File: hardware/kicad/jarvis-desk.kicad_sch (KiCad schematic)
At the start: 4 parts, among them J1 RJ12_6P6C, U1 Beetle_ESP32-C6

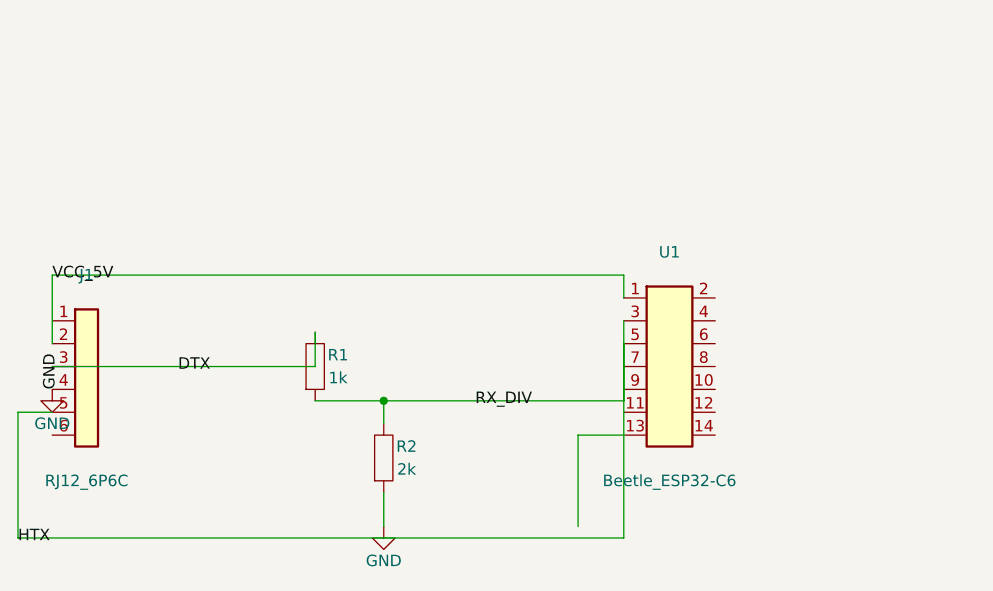
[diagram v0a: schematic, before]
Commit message: Rebuild PCB with official DFRobot Beetle ESP32-C6 footprint
- Copy official kicad_mod and kicad_sym from DFRobot to hardware/kicad/libs/
- Rewrite PCB (38x30mm board) using official 16-pin Beetle footprint
  with correct pad positions (2x8, 2.54mm pitch, 17.78mm row spacing)
- Update schematic to use official Beetle_ESP32-C6 symbol
- Route all nets: GND, VCC_5V, DTX→R1→R2 voltage divider→GPIO17,
  HTX→GPIO16, with back copper GND pour
- Change DESK_TX_PIN from 18 to 16 in config.h and config.example.h
  (GPIO18 not on Beetle headers; GPIO16 is pin 12, adjacent to GPIO17)
- Pin assignments: GPIO17 (pin 13) = RX, GPIO16 (pin 12) = TX

Co-authored-by: Copilot <223556219+Copilot@users.noreply.github.com>
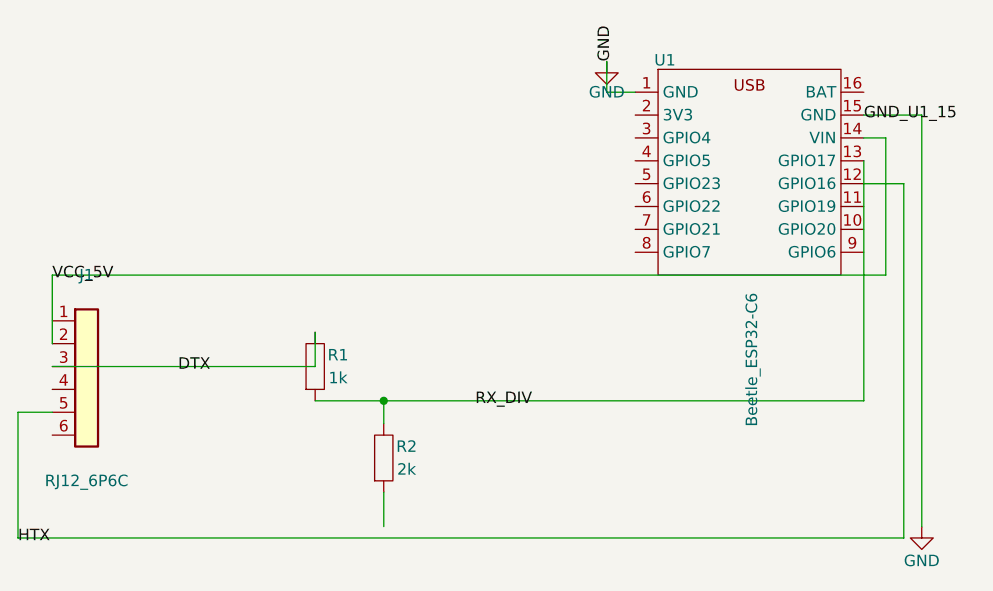
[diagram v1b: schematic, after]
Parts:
- U1: footprint Connector_PinHeader_2.54mm:PinHeader_2x07_P2.54mm_Vertical -> libs:Beetle_ESP32-C6; symbol Connector_Generic:Conn_02x07_Odd_Even -> beetle_esp32_c6:Beetle_ESP32-C6
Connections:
- net GND: now also U1.1 (GND), U1.15 (GND); no longer J1.4 (Pin_4), R2.2
- net HTX: now also U1.12 (GPIO16); no longer R1.2, R2.1, U1.3 (Pin_3), U1.5 (Pin_5)
- net VCC_5V: now also U1.14 (VIN); no longer U1.1 (Pin_1)
- net RX_DIV: now reaches U1.13 (GPIO17)
- net RX_DIV: now also R1.2, R2.1
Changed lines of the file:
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@@
   )
   (symbol
-    (lib_id "Connector_Generic:Conn_02x07_Odd_Even")
-    (at 139.7 88.9 0)
+    (lib_id "beetle_esp32_c6:Beetle_ESP32-C6")
+    (at 139.7 78.74 0)
     (unit 1)
     (exclude_from_sim no)
@@
     (on_board yes)
     (dnp no)
-    (property "Reference" "U1" (at 140.97 76.2 0) (effects (font (size 1.27 1.27))))
-    (property "Value" "Beetle_ESP32-C6" (at 140.97 101.6 0) (effects (font (size 1.27 1.27))))
-    (property "Footprint" "Connector_PinHeader_2.54mm:PinHeader_2x07_P2.54mm_Vertical" (at 139.7 88.9 0) (effects (font (size 1.27 1.27)) hide))
-    (property "Datasheet" "~" (at 139.7 88.9 0) (effects (font (size 1.27 1.27)) hide))
+    (property "Reference" "U1" (at 140.462 54.864 0) (effects (font (size 1.27 1.27))))
+    (property "Value" "Beetle_ESP32-C6" (at 150.114 88.138 90) (effects (font (size 1.27 1.27))))
+    (property "Footprint" "libs:Beetle_ESP32-C6" (at 139.7 72.39 0) (effects (font (size 1.27 1.27)) hide))
+    (property "Datasheet" "" (at 139.7 72.39 0) (effects (font (size 1.27 1.27)) hide))
     (pin "1")
     (pin "2")
@@
     (pin "13")
     (pin "14")
+    (pin "15")
+    (pin "16")
     (instances
       (project "jarvis-desk"
@@
   (symbol
     (lib_id "power:GND")
-    (at 72.39 91.44 0)
+    (at 134 55 0)
     (unit 1)
     (exclude_from_sim no)
@@
     (on_board yes)
     (dnp no)
-    (property "Reference" "#PWR01" (at 72.39 97.79 0) (effects (font (size 1.27 1.27)) hide))
-    (property "Value" "GND" (at 72.39 95.25 0) (effects (font (size 1.27 1.27))))
-    (property "Footprint" "" (at 72.39 91.44 0) (effects (font (size 1.27 1.27)) hide))
-    (property "Datasheet" "" (at 72.39 91.44 0) (effects (font (size 1.27 1.27)) hide))
+    (property "Reference" "#PWR01" (at 134 61.34 0) (effects (font (size 1.27 1.27)) hide))
+    (property "Value" "GND" (at 134 58.42 0) (effects (font (size 1.27 1.27))))
+    (property "Footprint" "" (at 134 55 0) (effects (font (size 1.27 1.27)) hide))
+    (property "Datasheet" "" (at 134 55 0) (effects (font (size 1.27 1.27)) hide))
     (pin "1")
     (instances
@@
   (symbol
     (lib_id "power:GND")
-    (at 109.22 106.68 0)
+    (at 169 106.68 0)
     (unit 1)
     (exclude_from_sim no)
@@
     (on_board yes)
     (dnp no)
-    (property "Reference" "#PWR02" (at 109.22 113.03 0) (effects (font (size 1.27 1.27)) hide))
-    (property "Value" "GND" (at 109.22 110.49 0) (effects (font (size 1.27 1.27))))
-    (property "Footprint" "" (at 109.22 106.68 0) (effects (font (size 1.27 1.27)) hide))
-    (property "Datasheet" "" (at 109.22 106.68 0) (effects (font (size 1.27 1.27)) hide))
+    (property "Reference" "#PWR02" (at 169 113.03 0) (effects (font (size 1.27 1.27)) hide))
+    (property "Value" "GND" (at 169 110.49 0) (effects (font (size 1.27 1.27))))
+    (property "Footprint" "" (at 169 106.68 0) (effects (font (size 1.27 1.27)) hide))
+    (property "Datasheet" "" (at 169 106.68 0) (effects (font (size 1.27 1.27)) hide))
     (pin "1")
     (instances
@@
     (stroke (width 0) (type default))
   )
-  (wire (pts (xy 109.22 92.71) (xy 135.89 92.71))
+  (wire (pts (xy 109.22 92.71) (xy 162.56 92.71))
     (stroke (width 0) (type default))
   )
-  (wire (pts (xy 135.89 92.71) (xy 135.89 86.36))
+  (wire (pts (xy 162.56 92.71) (xy 162.56 66.04))
     (stroke (width 0) (type default))
   )
@@
     (stroke (width 0) (type default))
   )
-  (wire (pts (xy 72.39 78.74) (xy 135.89 78.74))
+  (wire (pts (xy 72.39 78.74) (xy 165 78.74))
     (stroke (width 0) (type default))
   )
-  (wire (pts (xy 135.89 78.74) (xy 135.89 81.28))
+  (wire (pts (xy 165 78.74) (xy 165 63.5))
+    (stroke (width 0) (type default))
+  )
+  (wire (pts (xy 165 63.5) (xy 162.56 63.5))
     (stroke (width 0) (type default))
   )
@@
     (stroke (width 0) (type default))
   )
-  (wire (pts (xy 68.58 107.95) (xy 135.89 107.95))
+  (wire (pts (xy 68.58 107.95) (xy 167 107.95))
     (stroke (width 0) (type default))
   )
-  (wire (pts (xy 135.89 107.95) (xy 135.89 83.82))
+  (wire (pts (xy 167 107.95) (xy 167 68.58))
     (stroke (width 0) (type default))
   )
-  (wire (pts (xy 135.89 96.52) (xy 130.81 96.52))
+  (wire (pts (xy 167 68.58) (xy 162.56 68.58))
     (stroke (width 0) (type default))
   )
-  (wire (pts (xy 130.81 96.52) (xy 130.81 106.68))
+  (wire (pts (xy 162.56 60.96) (xy 169 60.96))
+    (stroke (width 0) (type default))
+  )
+  (wire (pts (xy 169 60.96) (xy 169 106.68))
+    (stroke (width 0) (type default))
+  )
+  (wire (pts (xy 137.16 58.42) (xy 134 58.42))
+    (stroke (width 0) (type default))
+  )
+  (wire (pts (xy 134 58.42) (xy 134 55))
     (stroke (width 0) (type default))
   )
@@
   )
   (label "GND"
-    (at 72.39 91.44 270)
+    (at 134 55 270)
     (effects (font (size 1.27 1.27)) (justify left))
   )
@@
     (effects (font (size 1.27 1.27)) (justify left))
   )
+  (label "GND_U1_15"
+    (at 162.56 60.96 0)
+    (effects (font (size 1.27 1.27)) (justify left))
+  )
